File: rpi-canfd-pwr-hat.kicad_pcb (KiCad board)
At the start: 4 copper layers, 65 x 56 mm, 89 parts, among them J1 Conn_01x02, J2 Conn_01x04_Pin, J3 Raspberry_Pi, J4 Conn_01x02, J5 Conn_01x02, U1 XC6206P332MR, U10 SN74LV1T125DBV, U11 SN74LV1T125DBV, U12 SN74LV1T125DBV, U13 SN74LV1T125DBV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

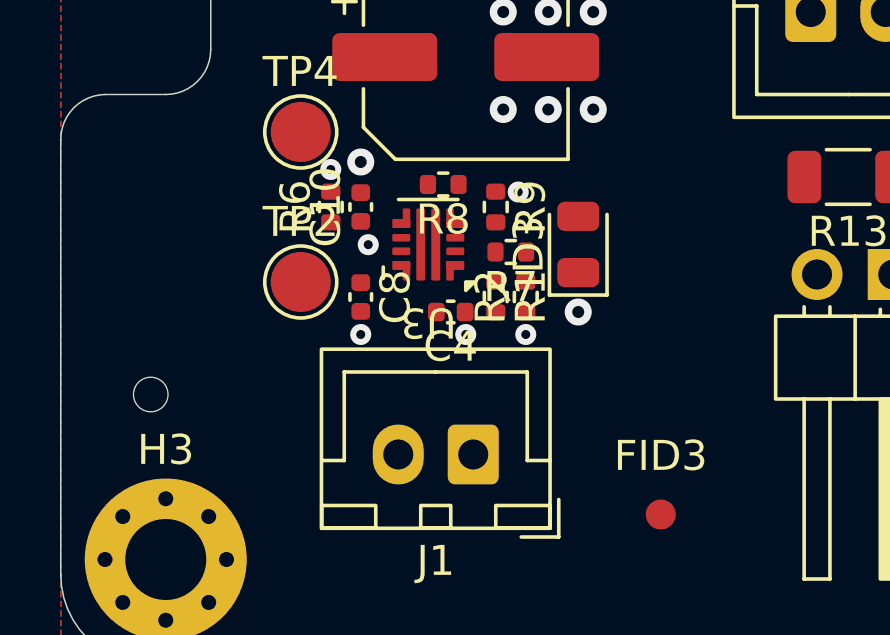
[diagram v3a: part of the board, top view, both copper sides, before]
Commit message: pcb: route input efuse
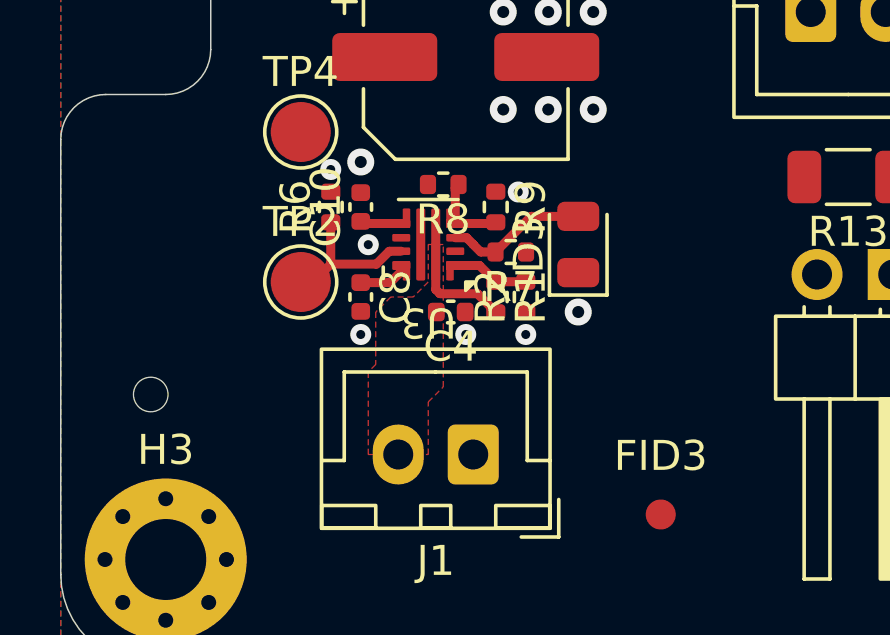
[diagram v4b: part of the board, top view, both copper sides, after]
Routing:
- net Net-(U3-ILM): track 0.00 -> 5.17 mm
- net Net-(D3-A): track 0.00 -> 4.79 mm
- net Net-(J1-Pin_2): track 0.00 -> 3.82 mm
- net Net-(U3-PGTH): track 0.00 -> 2.71 mm
- net Net-(U3-EN/UVLO): track 0.00 -> 2.57 mm
- net Net-(U3-ITIMER): track 0.00 -> 1.70 mm
- net Net-(U3-DVDT): track 0.00 -> 1.38 mm
- added copper zone on F.Cu, net Net-(J1-Pin_2)
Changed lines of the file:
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@@
+	)
+	(segment
+		(start 160 113.27)
+		(end 160.98 113.27)
+		(width 0.3)
+		(layer "F.Cu")
+		(net "Net-(U3-ITIMER)")
+	)
+	(segment
+		(start 161.35 112.9)
+		(end 161.35 112.7)
+		(width 0.3)
+		(layer "F.Cu")
+		(net "Net-(U3-ITIMER)")
+	)
+	(segment
+		(start 160.98 113.27)
+		(end 161.35 112.9)
+		(width 0.3)
+		(layer "F.Cu")
+		(net "Net-(U3-ITIMER)")
 	)
 	(segment
@@
 	)
 	(segment
+		(start 162.64 113.64)
+		(end 162.5 113.5)
+		(width 0.3)
+		(layer "F.Cu")
+		(net "Net-(J1-Pin_2)")
+	)
+	(segment
+		(start 163.89 113.64)
+		(end 162.64 113.64)
+		(width 0.3)
+		(layer "F.Cu")
+		(net "Net-(J1-Pin_2)")
+	)
+	(segment
+		(start 164.5 114.26)
+		(end 164.5 114.25)
+		(width 0.3)
+		(layer "F.Cu")
+		(net "Net-(J1-Pin_2)")
+	)
+	(segment
+		(start 164.5 114.25)
+		(end 163.89 113.64)
+		(width 0.3)
+		(layer "F.Cu")
+		(net "Net-(J1-Pin_2)")
+	)
+	(segment
+		(start 162.5 113.5)
+		(end 162.5 112)
+		(width 0.3)
+		(layer "F.Cu")
+		(net "Net-(J1-Pin_2)")
+	)
+	(segment
 		(start 203.9 86.6)
 		(end 203.73 86.77)
@@
 	)
 	(segment
+		(start 160.950389 112.225)
+		(end 160.519879 112.65551)
+		(width 0.3)
+		(layer "F.Cu")
+		(net "Net-(U3-ILM)")
+	)
+	(segment
+		(start 159 112.65551)
+		(end 159 111.26)
+		(width 0.3)
+		(layer "F.Cu")
+		(net "Net-(U3-ILM)")
+	)
+	(segment
+		(start 158 113.25)
+		(end 158.40551 113.25)
+		(width 0.3)
+		(layer "F.Cu")
+		(net "Net-(U3-ILM)")
+	)
+	(segment
+		(start 158.40551 113.25)
+		(end 159 112.65551)
+		(width 0.3)
+		(layer "F.Cu")
+		(net "Net-(U3-ILM)")
+	)
+	(segment
+		(start 160.519879 112.65551)
+		(end 159 112.65551)
+		(width 0.3)
+		(layer "F.Cu")
+		(net "Net-(U3-ILM)")
+	)
+	(segment
+		(start 161.35 112.225)
+		(end 160.950389 112.225)
+		(width 0.3)
+		(layer "F.Cu")
+		(net "Net-(U3-ILM)")
+	)
+	(segment
+		(start 163.15 111.3)
+		(end 164.46 111.3)
+		(width 0.3)
+		(layer "F.Cu")
+		(net "Net-(U3-PGTH)")
+	)
+	(segment
+		(start 164.46 111.3)
+		(end 164.5 111.26)
+		(width 0.3)
+		(layer "F.Cu")
+		(net "Net-(U3-PGTH)")
+	)
+	(segment
+		(start 163.15 111.3)
+		(end 163.15 110.11)
+		(width 0.3)
+		(layer "F.Cu")
+		(net "Net-(U3-PGTH)")
+	)
+	(segment
+		(start 163.15 110.11)
+		(end 163.26 110)
+		(width 0.3)
+		(layer "F.Cu")
+		(net "Net-(U3-PGTH)")
+	)
+	(segment
 		(start 194.775 85.635)
 		(end 192.21 85.635)
@@
 	)
 	(segment
+		(start 160.07 111.3)
+		(end 160 111.23)
+		(width 0.3)
+		(layer "F.Cu")
+		(net "Net-(U3-DVDT)")
+	)
+	(segment
+		(start 161.35 111.3)
+		(end 160.07 111.3)
+		(width 0.3)
+		(layer "F.Cu")
+		(net "Net-(U3-DVDT)")
+	)
+	(segment
 		(start 207.73 72.23)
 		(end 206.63 72.23)
@@
 	)
 	(segment
+		(start 163.96 112.7)
+		(end 163.15 112.7)
+		(width 0.3)
+		(layer "F.Cu")
+		(net "Net-(U3-EN{slash}UVLO)")
+	)
+	(segment
+		(start 164.5 113.24)
+		(end 163.96 112.7)
+		(width 0.3)
+		(layer "F.Cu")
+		(net "Net-(U3-EN{slash}UVLO)")
+	)
+	(segment
+		(start 165.5 113.24)
+		(end 164.5 113.24)
+		(width 0.3)
+		(layer "F.Cu")
+		(net "Net-(U3-EN{slash}UVLO)")
+	)
+	(segment
 		(start 203.75 88.5)
 		(end 204.3 87.95)
@@
 		(layer "F.Cu")
 		(net "Net-(U6-REGOUT)")
+	)
+	(segment
+		(start 165.6775 111.0625)
+		(end 167.25 111.0625)
+		(width 0.3)
+		(layer "F.Cu")
+		(net "Net-(D3-A)")
+	)
+	(segment
+		(start 163.75 112)
+		(end 163.75 111.996664)
+		(width 0.3)
+		(layer "F.Cu")
+		(net "Net-(D3-A)")
+	)
+	(segment
+		(start 163.528336 111.775)
+		(end 163.15 111.775)
+		(width 0.3)
+		(layer "F.Cu")
+		(net "Net-(D3-A)")
+	)
+	(segment
+		(start 164.49 112.25)
+		(end 164 112.25)
+		(width 0.3)
+		(layer "F.Cu")
+		(net "Net-(D3-A)")
+	)
+	(segment
+		(start 164 112.25)
+		(end 163.75 112)
+		(width 0.3)
+		(layer "F.Cu")
+		(net "Net-(D3-A)")
+	)
+	(segment
+		(start 164.49 112.25)
+		(end 165.6775 111.0625)
+		(width 0.3)
+		(layer "F.Cu")
+		(net "Net-(D3-A)")
+	)
+	(segment
+		(start 163.75 111.996664)
+		(end 163.528336 111.775)
+		(width 0.3)
+		(layer "F.Cu")
+		(net "Net-(D3-A)")
 	)
 	(segment
@@
 			)
 		)
+	)
+	(zone
+		(net "Net-(J1-Pin_2)")
+		(layer "F.Cu")
+		(hatch edge 0.5)
+		(priority 2)
+		(connect_pads yes
+			(clearance 0.2)
+		)
+		(min_thickness 0.15)
+		(fill yes
+			(thermal_gap 0.5)
+			(thermal_bridge_width 0.5)
+			(island_removal_mode 0)
+		)
+		(polygon
+			(pts
+				(xy 162.25 119) (xy 162.25 117.25) (xy 162.75 116.75) (xy 162.75 112) (xy 162.25 112) (xy 162.25 113.25)
+				(xy 161.75 113.75) (xy 161 113.75) (xy 160.5 114.25) (xy 160.5 116) (xy 160.25 116.25) (xy 160.25 119)
+			)
+		)

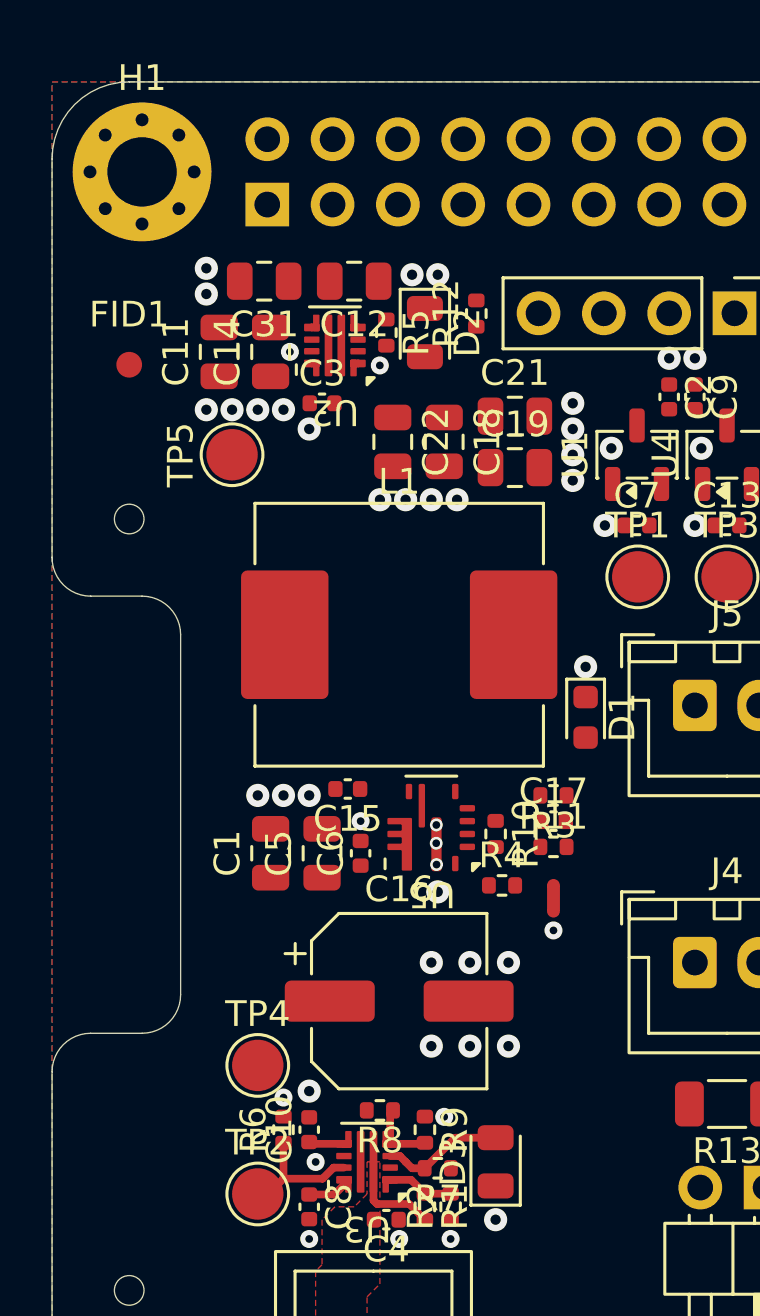
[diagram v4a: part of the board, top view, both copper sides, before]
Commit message: pcb: route rpi power path
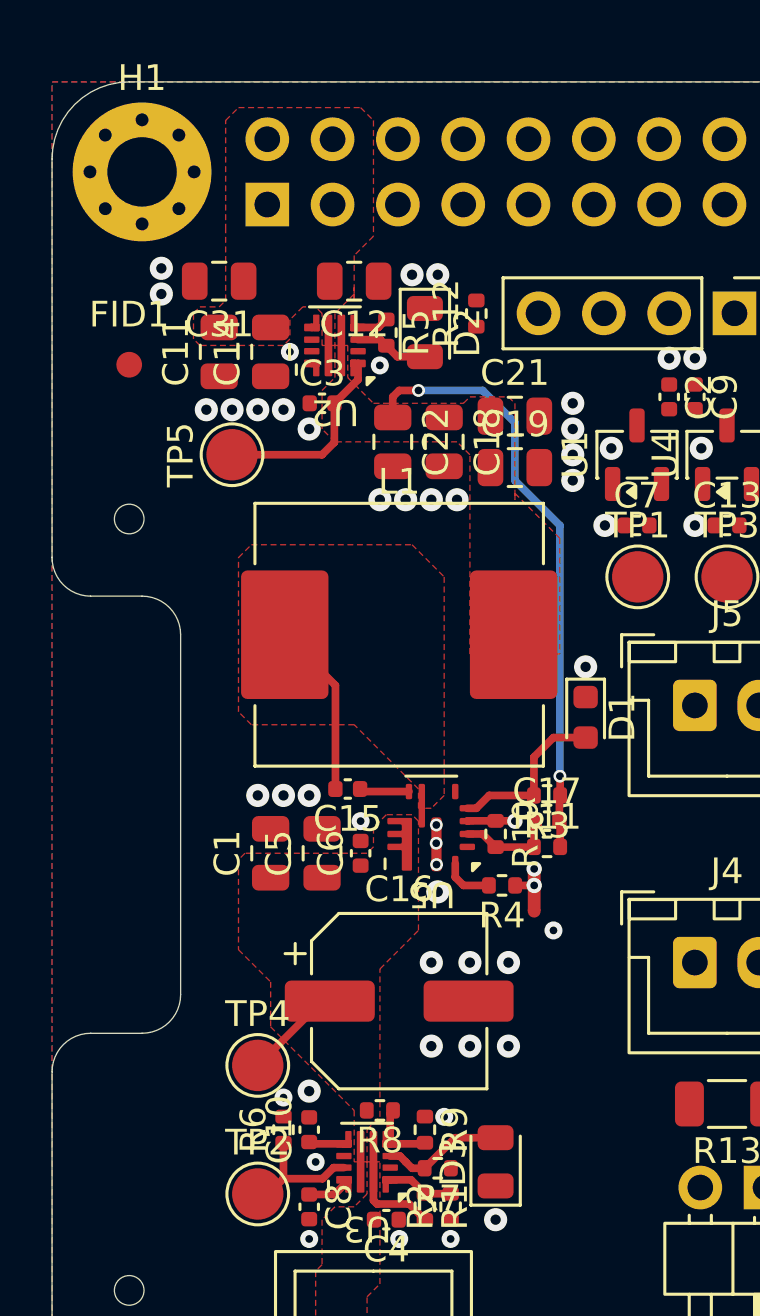
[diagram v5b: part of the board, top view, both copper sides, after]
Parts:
- moved C31 1.75 mm to (156.5, 77.8)
- moved NT1 0.75 mm to (168.8, 101.8)
- moved C17 0.25 mm to (169.2, 98.8)
- moved R11 0.25 mm to (169.2, 99.8)
- moved R3 0.25 mm to (169.2, 97.8)
- turned R4 to 180 degrees
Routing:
- net +Vbuck: track 0.00 -> 31.1 mm, vias 0 -> 2
- net Net-(U5-SW): track 0.00 -> 6.82 mm
- net Net-(D1-A): track 0.00 -> 6.61 mm
- net +12V: track 0.00 -> 3.84 mm
- net Net-(U5-FB): track 0.00 -> 3.82 mm
- net AGND: track 0.00 -> 3.24 mm, vias 0 -> 3
- net Net-(D2-A): track 0.00 -> 2.87 mm
- net Net-(U5-MODE): track 0.00 -> 1.97 mm
- net Net-(U5-BOOT): track 0.00 -> 1.94 mm
- net +5V: track 0.00 -> 1.23 mm
- added copper zone on F.Cu, net +12V
- added copper zone on F.Cu, net +5V
- added copper zone on F.Cu, net +Vbuck
- added copper zone on F.Cu, net Net-(U5-SW)

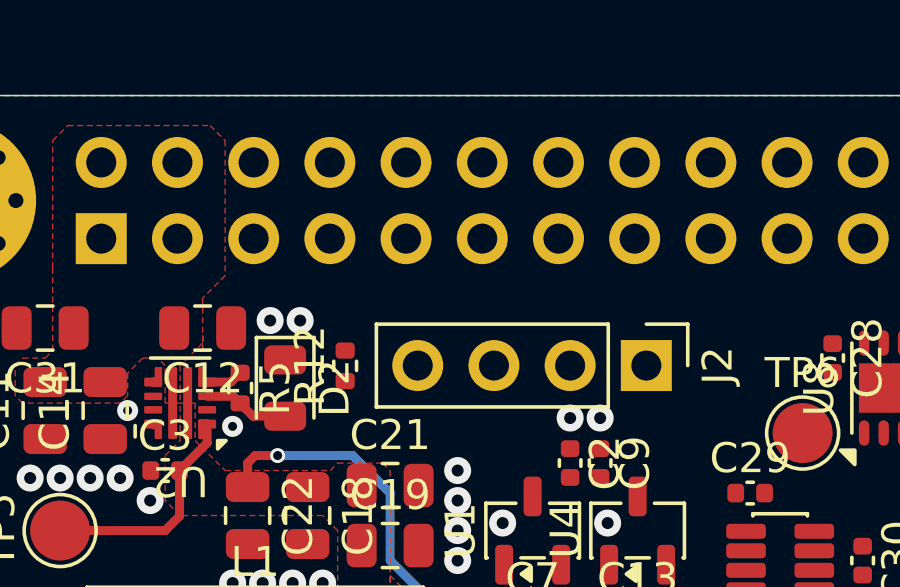
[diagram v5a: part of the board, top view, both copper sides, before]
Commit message: pcb: route uart
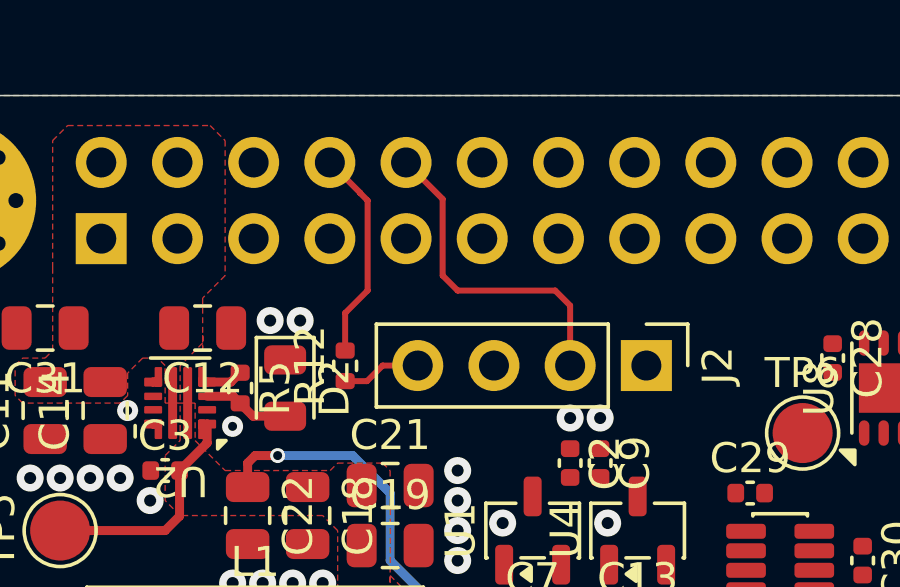
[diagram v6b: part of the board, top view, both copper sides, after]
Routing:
- net /U0RXD: track 0.00 -> 10.9 mm
- net /U0TXD: track 0.00 -> 7.10 mm
- net Net-(J2-Pin_4): track 0.00 -> 2.64 mm
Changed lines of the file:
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@@
+	)
+	(segment
+		(start 166.5 79.52)
+		(end 167.23 79.52)
+		(width 0.2)
+		(layer "F.Cu")
+		(net "Net-(J2-Pin_4)")
+	)
+	(segment
+		(start 167.75 79)
+		(end 168.92 79)
+		(width 0.2)
+		(layer "F.Cu")
+		(net "Net-(J2-Pin_4)")
+	)
+	(segment
+		(start 167.23 79.52)
+		(end 167.75 79)
+		(width 0.2)
+		(layer "F.Cu")
+		(net "Net-(J2-Pin_4)")
+	)
+	(segment
+		(start 167.25 73.5)
+		(end 167.25 76.5)
+		(width 0.2)
+		(layer "F.Cu")
+		(net "/U0TXD")
+	)
+	(segment
+		(start 165.99 72.23)
+		(end 167 73.24)
+		(width 0.2)
+		(layer "F.Cu")
+		(net "/U0TXD")
+	)
+	(segment
+		(start 167.25 76.5)
+		(end 166.5 77.25)
+		(width 0.2)
+		(layer "F.Cu")
+		(net "/U0TXD")
+	)
+	(segment
+		(start 166.5 77.25)
+		(end 166.5 78.5)
+		(width 0.2)
+		(layer "F.Cu")
+		(net "/U0TXD")
+	)
+	(segment
+		(start 167 73.24)
+		(end 167 73.25)
+		(width 0.2)
+		(layer "F.Cu")
+		(net "/U0TXD")
+	)
+	(segment
+		(start 167 73.25)
+		(end 167.25 73.5)
+		(width 0.2)
+		(layer "F.Cu")
+		(net "/U0TXD")
 	)
 	(segment
@@
 	)
 	(segment
+		(start 174 79)
+		(end 174 77)
+		(width 0.2)
+		(layer "F.Cu")
+		(net "/U0RXD")
+	)
+	(segment
+		(start 174 77)
+		(end 173.5 76.5)
+		(width 0.2)
+		(layer "F.Cu")
+		(net "/U0RXD")
+	)
+	(segment
+		(start 173.5 76.5)
+		(end 170.25 76.5)
+		(width 0.2)
+		(layer "F.Cu")
+		(net "/U0RXD")
+	)
+	(segment
+		(start 170.25 76.5)
+		(end 169.75 76)
+		(width 0.2)
+		(layer "F.Cu")
+		(net "/U0RXD")
+	)
+	(segment
+		(start 169.75 73.45)
+		(end 168.53 72.23)
+		(width 0.2)
+		(layer "F.Cu")
+		(net "/U0RXD")
+	)
+	(segment
+		(start 169.75 76)
+		(end 169.75 73.45)
+		(width 0.2)
+		(layer "F.Cu")
+		(net "/U0RXD")
+	)
+	(segment

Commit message: pcb: route ldos
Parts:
- moved TP1 0.25 mm to (172.8, 89.5)
- moved TP3 0.25 mm to (176.2, 89.5)
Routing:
- net +5V: track 1.23 -> 26.6 mm
- net +1V8: track 1.32 -> 5.58 mm
- net +3V3: track 10.4 -> 14.7 mm
- net GND: track 6.44 -> 7.97 mm, vias 76 -> 77
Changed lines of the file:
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@@
 	(footprint "TestPoint:TestPoint_Pad_D2.0mm"
 		(layer "F.Cu")
-		(at 172.7775 89.25)
+		(at 172.7775 89.5)
 		(descr "SMD pad as test Point, diameter 2.0mm")
 		(tags "test point SMD pad")
@@
 	(footprint "TestPoint:TestPoint_Pad_D2.0mm"
 		(layer "F.Cu")
-		(at 176.25 89.25)
+		(at 176.25 89.5)
 		(descr "SMD pad as test Point, diameter 2.0mm")
 		(tags "test point SMD pad")
@@
 	)
 	(segment
+		(start 160.1 80.475)
+		(end 160.1 80.025)
+		(width 0.3)
+		(layer "F.Cu")
+		(net "GND")
+	)
+	(segment
 		(start 188.2 85.05)
 		(end 188.2 85.95)
@@
 	)
 	(segment
+		(start 161.9 80.475)
+		(end 162.209128 80.475)
+		(width 0.2)
+		(layer "F.Cu")
+		(net "GND")
+	)
+	(segment
 		(start 186.8 83.371099)
 		(end 186.338833 82.909932)
@@
 	)
 	(segment
+		(start 162.209128 80.475)
+		(end 162.74703 81.012902)
+		(width 0.2)
+		(layer "F.Cu")
+		(net "GND")
+	)
+	(segment
 		(start 188.2 85.05)
 		(end 188.2 85.8)
@@
 		(net "GND")
 	)
+	(segment
+		(start 162.74703 81.012902)
+		(end 162.74703 81.027002)
+		(width 0.2)
+		(layer "F.Cu")
+		(net "GND")
+	)
 	(via
 		(at 171.75 84.25)
@@
 	)
 	(via
+		(at 158.314272 80.527047)
+		(size 0.5)
+		(drill 0.3)
+		(layers "F.Cu" "B.Cu")
+		(free yes)
+		(net "GND")
+	)
+	(via
 		(at 160 83.5)
 		(size 0.9)
@@
 	)
 	(segment
+		(start 172.7775 88.2225)
+		(end 172.7775 89.5)
+		(width 0.3)
+		(layer "F.Cu")
+		(net "+3V3")
+	)
+	(segment
 		(start 199.725 86.905)
 		(end 199.725 85.635)
@@
 	)
 	(segment
+		(start 173.23 87.77)
+		(end 172.7775 88.2225)
+		(width 0.3)
+		(layer "F.Cu")
+		(net "+3V3")
+	)
+	(segment
+		(start 173.7 85.6375)
+		(end 173.7 86.78)
+		(width 0.3)
+		(layer "F.Cu")
+		(net "+3V3")
+	)
+	(segment
+		(start 173.7 86.78)
+		(end 173.23 87.25)
+		(width 0.3)
+		(layer "F.Cu")
+		(net "+3V3")
+	)
+	(segment
 		(start 194.775 86.905)
 		(end 192.18 86.905)
@@
 	)
 	(segment
+		(start 173.23 87.25)
+		(end 173.23 87.77)
+		(width 0.3)
+		(layer "F.Cu")
+		(net "+3V3")
+	)
+	(segment
 		(start 194.71 86.97)
 		(end 194.775 86.905)
@@
 	)
 	(segment
+		(start 166.75 81.25)
+		(end 165.75 80.25)
+		(width 0.3)
+		(layer "F.Cu")
+		(net "+5V")
+	)
+	(segment
+		(start 172.75 83.3625)
+		(end 172.75 82)
+		(width 0.3)
+		(layer "F.Cu")
+		(net "+5V")
+	)
+	(segment
+		(start 173.3675 83.3625)
+		(end 174 82.73)
+		(width 0.3)
+		(layer "F.Cu")
+		(net "+5V")
+	)
+	(segment
+		(start 175.6325 83.3625)
+		(end 175.26 82.99)
+		(width 0.3)
+		(layer "F.Cu")
+		(net "+5V")
+	)
+	(segment
+		(start 175 82.73)
+		(end 174 82.73)
+		(width 0.3)
+		(layer "F.Cu")
+		(net "+5V")
+	)
+	(segment
+		(start 172 81.25)
+		(end 166.75 81.25)
+		(width 0.3)
+		(layer "F.Cu")
+		(net "+5V")
+	)
+	(segment
 		(start 161.9 79.55)
 		(end 162.69 79.55)
@@
 	)
 	(segment
+		(start 161 76.25)
+		(end 160.8 76.45)
+		(width 0.3)
+		(layer "F.Cu")
+		(net "+5V")
+	)
+	(segment
+		(start 172.75 82)
+		(end 172 81.25)
+		(width 0.3)
+		(layer "F.Cu")
+		(net "+5V")
+	)
+	(segment
+		(start 160.8 77.75)
+		(end 161.75 78.7)
+		(width 0.3)
+		(layer "F.Cu")
+		(net "+5V")
+	)
+	(segment
+		(start 161.75 78.7)
+		(end 161.75 79.4)
+		(width 0.3)
+		(layer "F.Cu")
+		(net "+5V")
+	)
+	(segment
+		(start 161.75 79.4)
+		(end 161.9 79.55)
+		(width 0.3)
+		(layer "F.Cu")
+		(net "+5V")
+	)
+	(segment
+		(start 176.25 83.3625)
+		(end 175.6325 83.3625)
+		(width 0.3)
+		(layer "F.Cu")
+		(net "+5V")
+	)
+	(segment
+		(start 172.75 83.3625)
+		(end 173.3675 83.3625)
+		(width 0.3)
+		(layer "F.Cu")
+		(net "+5V")
+	)
+	(segment
+		(start 165.75 76.75)
+		(end 165.25 76.25)
+		(width 0.3)
+		(layer "F.Cu")
+		(net "+5V")
+	)
+	(segment
+		(start 165.75 80.25)
+		(end 165.75 76.75)
+		(width 0.3)
+		(layer "F.Cu")
+		(net "+5V")
+	)
+	(segment
+		(start 165.25 76.25)
+		(end 161 76.25)
+		(width 0.3)
+		(layer "F.Cu")
+		(net "+5V")
+	)
+	(segment
+		(start 160.8 76.45)
+		(end 160.8 77.75)
+		(width 0.3)
+		(layer "F.Cu")
+		(net "+5V")
+	)
+	(segment
+		(start 175.26 82.99)
+		(end 175 82.73)
+		(width 0.3)
+		(layer "F.Cu")
+		(net "+5V")
+	)
+	(segment
 		(start 162.64 113.64)
 		(end 162.5 113.5)
@@
 	)
 	(segment
+		(start 177.2 85.6375)
+		(end 177.2 86.78)
+		(width 0.3)
+		(layer "F.Cu")
+		(net "+1V8")
+	)
+	(segment
+		(start 176.25 88.25)
+		(end 176.25 89.5)
+		(width 0.3)
+		(layer "F.Cu")
+		(net "+1V8")
+	)
+	(segment
+		(start 176.73 87.77)
+		(end 176.25 88.25)
+		(width 0.3)
+		(layer "F.Cu")
+		(net "+1V8")
+	)
+	(segment
 		(start 203.9 86.6)
 		(end 203.73 86.77)
@@
 		(layer "F.Cu")
 		(net "+1V8")
+	)
+	(segment
+		(start 176.73 87.25)
+		(end 176.73 87.77)
+		(width 0.3)
+		(layer "F.Cu")
+		(net "+1V8")
+	)
+	(segment
+		(start 177.2 86.78)
+		(end 176.73 87.25)
+		(width 0.3)
+		(layer "F.Cu")
+		(net "+1V8")

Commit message: pcb: route can
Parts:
- moved C26 0.33 mm to (185.7, 84.7)
- moved C27 0.33 mm to (189.7, 84.7)
- moved Y1 0.33 mm to (187.7, 84.7)
- moved C30 0.25 mm to (183.8, 85.8)
- moved TP6 0.25 mm to (181.8, 81.5)
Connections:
- J3 pad 18: /~{CAN_INT} -> unconnected-(J3-GPIO24/SDIO_DAT0-Pad18)
- J3 pad 26: unconnected-(J3-~{CE1}_SPI0/GPIO07-Pad26) -> /~{CAN_INT}
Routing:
- net /CANL: track 0.00 -> 32.6 mm
- net /CANH: track 0.00 -> 25.5 mm
- net /~{SPI_CS}: track 0.00 -> 17.3 mm
- net /~{CAN_INT}: track 0.00 -> 11.8 mm, vias 0 -> 1
- net /SPI_MOSI: track 0.00 -> 9.06 mm
- net /CAN_TX: track 0.00 -> 8.20 mm
- net /CAN_RX: track 0.00 -> 4.87 mm
- net Net-(U8-CLKO/SOF): track 0.00 -> 4.41 mm, vias 0 -> 2
- net +3V3: track 14.7 -> 19.0 mm
- net /SPI_MISO: track 0.00 -> 4.03 mm
- net /SPI_SCLK: track 0.00 -> 3.52 mm
- net Net-(JP2-B): track 0.00 -> 3.43 mm
- net GND: vias 77 -> 80
